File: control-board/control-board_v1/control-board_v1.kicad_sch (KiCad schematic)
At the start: 57 parts, among them J1 Barrel_Jack, J2 Header-M_2x6, J3 Header-M_2x6, J4 Header-M_2x6, J5 Header-M_2x6, J6 Header_1x8, J7 Header_1x8, J8 Header_1x10, J9 Header_1x8, Q1 PMOS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

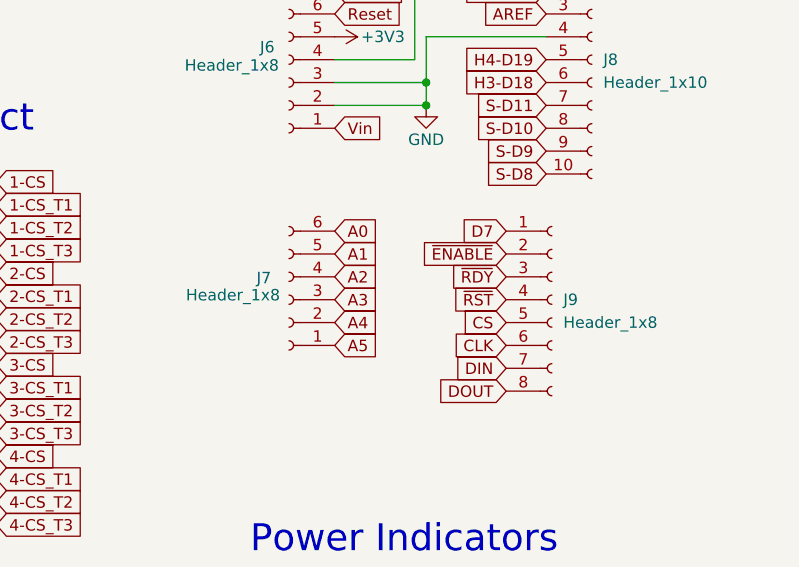
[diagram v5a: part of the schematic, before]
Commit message: pulldown resistor
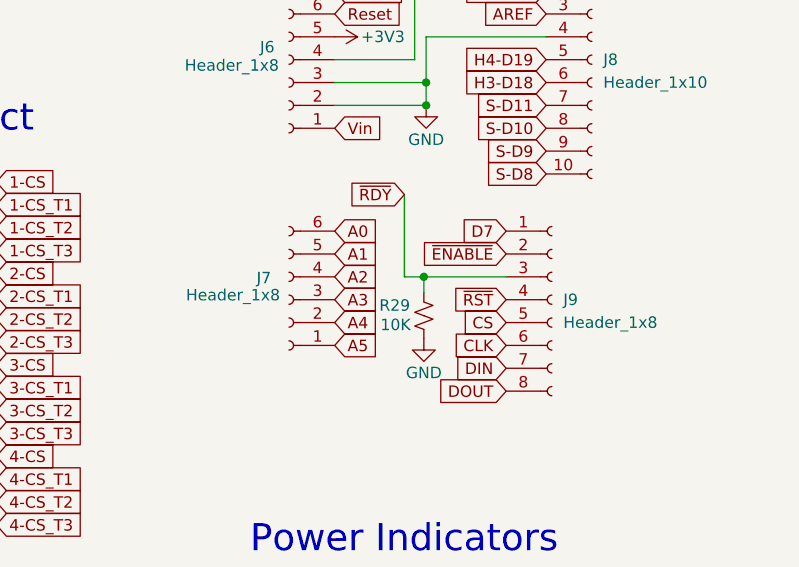
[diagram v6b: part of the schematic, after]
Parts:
- added R29: 10K, Resistor_SMD:R_0805_2012Metric, symbol Device:R_Small_US
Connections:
- net GND: now also R29.2
- net ~{RDY}: now also R29.1
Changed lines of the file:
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@@
   (junction (at 252.349 82.169) (diameter 0) (color 0 0 0 0)
   )
+  (junction (at 252.095 101.219) (diameter 0) (color 0 0 0 0)
+  )
   (junction (at 187.452 91.948) (diameter 0) (color 0 0 0 0)
   )
   (no_connect (at 100.457 118.491))
+  (wire (pts (xy 249.936 101.219) (xy 252.095 101.219))
+    (stroke (width 0) (type default))
+  )
   (wire (pts (xy 179.197 91.948) (xy 178.435 91.948))
     (stroke (width 0) (type default))
@@
     (stroke (width 0) (type default))
   )
+  (wire (pts (xy 252.095 101.219) (xy 261.239 101.219))
+    (stroke (width 0) (type default))
+  )
   (wire (pts (xy 185.928 127.508) (xy 187.452 127.508))
     (stroke (width 0) (type default))
@@
     (stroke (width 0) (type default))
   )
+  (wire (pts (xy 252.095 102.997) (xy 252.095 101.219))
+    (stroke (width 0) (type default))
+  )
   (wire (pts (xy 252.349 82.169) (xy 252.349 79.629))
     (stroke (width 0) (type default))
@@
     (stroke (width 0) (type default))
   )
+  (wire (pts (xy 249.936 92.075) (xy 249.936 101.219))
+    (stroke (width 0) (type default))
+  )
   (wire (pts (xy 266.827 31.369) (xy 270.002 31.369))
     (stroke (width 0) (type default))
@@
     )
   )
-  (global_label "~{RDY}" (shape input) (at 261.239 101.219 180) (fields_autoplaced)
+  (global_label "~{RDY}" (shape input) (at 249.936 92.075 180) (fields_autoplaced)
     (effects (font (size 1.27 1.27)) (justify right))
-    (property "Intersheetrefs" "${INTERSHEET_REFS}" (at 254.6252 101.219 0)
+    (property "Intersheetrefs" "${INTERSHEET_REFS}" (at 243.3222 92.075 0)
       (effects (font (size 1.27 1.27)) (justify right) hide)
     )
@@
     )
   )
+  (symbol (lib_id "power:GND") (at 252.095 108.077 0) (unit 1)
+    (in_bom yes) (on_board yes) (dnp no)
+    (property "Reference" "#PWR046" (at 252.095 114.427 0)
+      (effects (font (size 1.27 1.27)) hide)
+    )
+    (property "Value" "GND" (at 252.095 111.887 0)
+      (effects (font (size 1.27 1.27)))
+    )
+    (property "Footprint" "" (at 252.095 108.077 0)
+      (effects (font (size 1.27 1.27)) hide)
+    )
+    (property "Datasheet" "" (at 252.095 108.077 0)
+      (effects (font (size 1.27 1.27)) hide)
+    )
+    (pin "1")
+    (instances
+      (project "control-board_v1"
+        (path "/5ea0e920-d127-456d-9ad4-df9bbc649b9b"
+          (reference "#PWR046") (unit 1)
+        )
+      )
+      (project "arduino_uno"
+        (path "/b1128066-0aeb-425d-915d-968e839977c3"
+          (reference "#PWR046") (unit 1)
+        )
+      )
+    )
+  )
   (symbol (lib_id "Connector:Conn_01x08_Socket") (at 237.109 77.089 180) (unit 1)
     (in_bom yes) (on_board yes) (dnp no)
@@
         )
       )
+    )
+  )
+  (symbol (lib_id "Device:R_Small_US") (at 252.095 105.537 0) (unit 1)
+    (in_bom yes) (on_board yes) (dnp no)
+    (property "Reference" "R29" (at 247.142 104.394 0)
+      (effects (font (size 1.27 1.27)) (justify left))
+    )
+    (property "Value" "10K" (at 247.269 106.553 0)
+      (effects (font (size 1.27 1.27)) (justify left))
+    )
+    (property "Footprint" "Resistor_SMD:R_0805_2012Metric" (at 252.095 105.537 0)
+      (effects (font (size 1.27 1.27)) hide)
+    )
+    (property "Datasheet" "~" (at 252.095 105.537 0)
+      (effects (font (size 1.27 1.27)) hide)
+    )
+    (pin "1")
+    (pin "2")
+    (instances
+      (project "control-board_v1"
+        (path "/5ea0e920-d127-456d-9ad4-df9bbc649b9b"
+          (reference "R29") (unit 1)
+        )
+      )

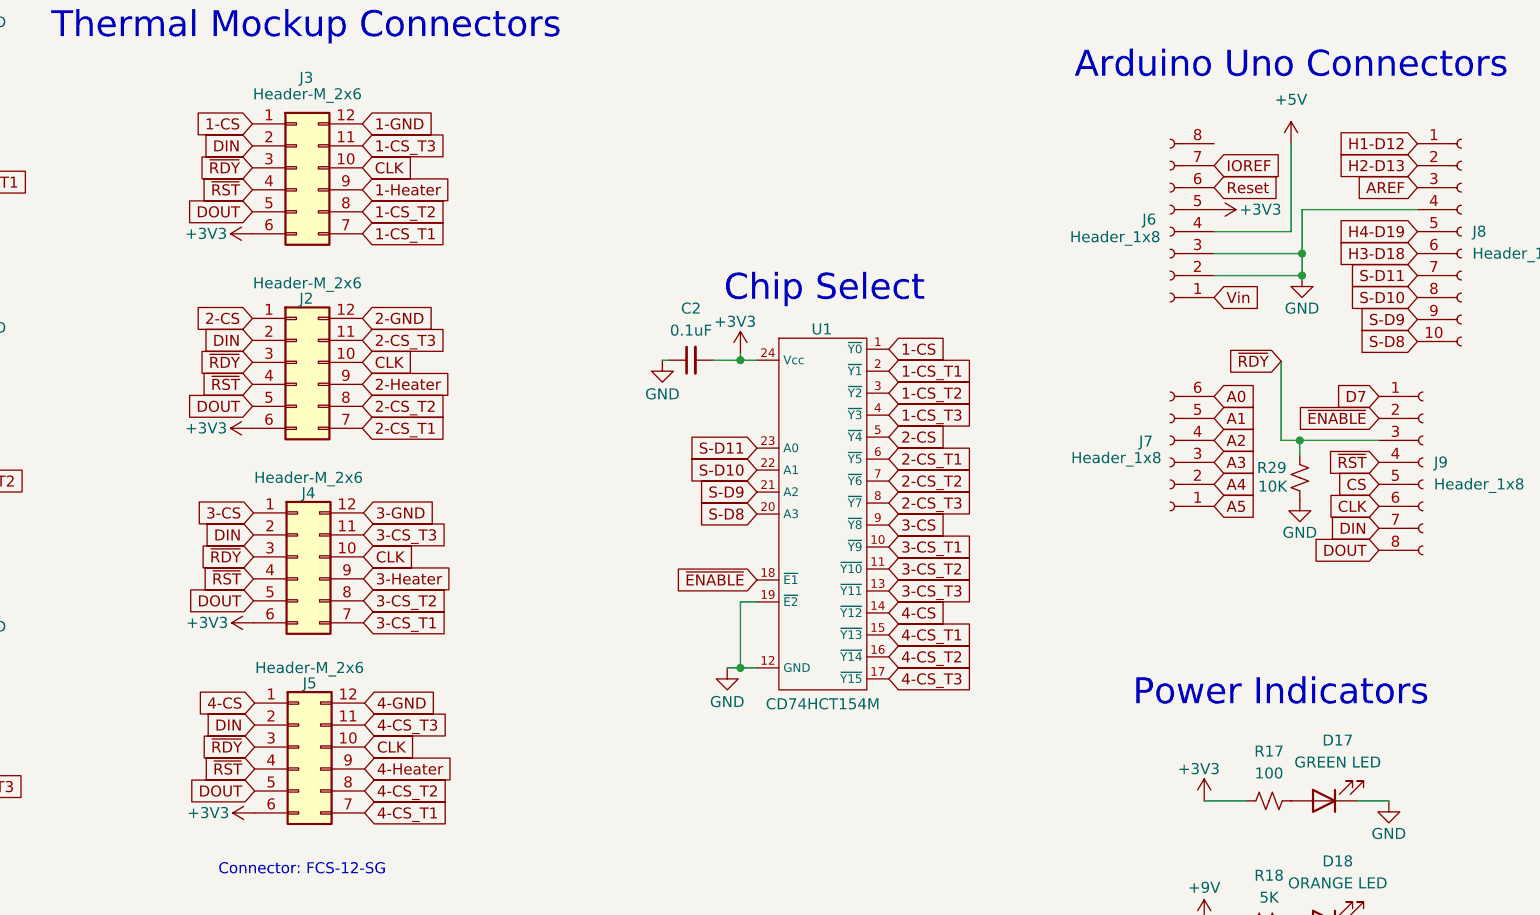
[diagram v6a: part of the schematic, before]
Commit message: fixed RDYB logic in pcb
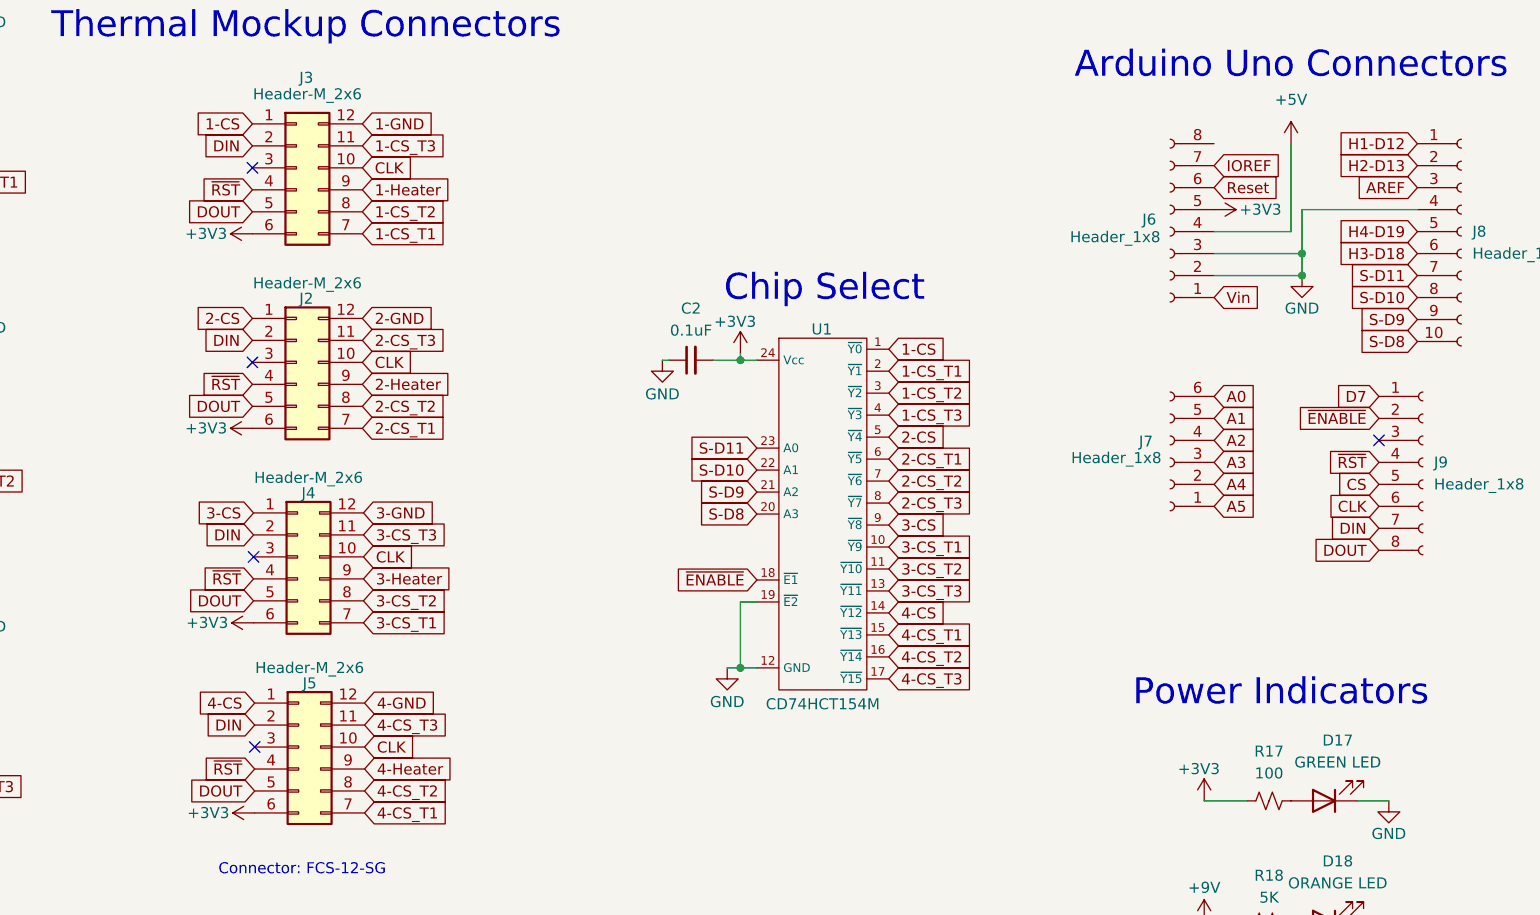
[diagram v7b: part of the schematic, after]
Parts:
- removed R29: 10K, Resistor_SMD:R_0805_2012Metric, symbol Device:R_Small_US
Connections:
- removed net ~{RDY}: J2.3 (Pin_3), J3.3 (Pin_3), J4.3 (Pin_3), J5.3 (Pin_3), J9.3 (Pin_3)
- no-connect marks 1 -> 6
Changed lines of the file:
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@@
   (junction (at 252.349 82.169) (diameter 0) (color 0 0 0 0)
   )
-  (junction (at 252.095 101.219) (diameter 0) (color 0 0 0 0)
-  )
   (junction (at 187.452 91.948) (diameter 0) (color 0 0 0 0)
   )
   (no_connect (at 100.457 118.491))
-  (wire (pts (xy 249.936 101.219) (xy 252.095 101.219))
-    (stroke (width 0) (type default))
-  )
+  (no_connect (at 131.064 69.723))
+  (no_connect (at 131.191 114.681))
+  (no_connect (at 131.318 136.652))
+  (no_connect (at 261.239 101.219))
+  (no_connect (at 131.064 92.202))
   (wire (pts (xy 179.197 91.948) (xy 178.435 91.948))
     (stroke (width 0) (type default))
@@
     (stroke (width 0) (type default))
   )
-  (wire (pts (xy 252.095 101.219) (xy 261.239 101.219))
-    (stroke (width 0) (type default))
-  )
   (wire (pts (xy 185.928 127.508) (xy 187.452 127.508))
     (stroke (width 0) (type default))
@@
     (stroke (width 0) (type default))
   )
-  (wire (pts (xy 252.095 102.997) (xy 252.095 101.219))
-    (stroke (width 0) (type default))
-  )
   (wire (pts (xy 252.349 82.169) (xy 252.349 79.629))
     (stroke (width 0) (type default))
@@
     (stroke (width 0) (type default))
   )
-  (wire (pts (xy 249.936 92.075) (xy 249.936 101.219))
-    (stroke (width 0) (type default))
-  )
   (wire (pts (xy 266.827 31.369) (xy 270.002 31.369))
     (stroke (width 0) (type default))
@@
     )
   )
-  (global_label "~{RDY}" (shape input) (at 131.064 69.723 180) (fields_autoplaced)
-    (effects (font (size 1.27 1.27)) (justify right))
-    (property "Intersheetrefs" "${INTERSHEET_REFS}" (at 124.4502 69.723 0)
-      (effects (font (size 1.27 1.27)) (justify right) hide)
-    )
-  )
   (global_label "S-D10" (shape input) (at 265.684 84.709 180) (fields_autoplaced)
     (effects (font (size 1.27 1.27)) (justify right))
@@
     )
   )
-  (global_label "~{RDY}" (shape input) (at 131.318 136.652 180) (fields_autoplaced)
-    (effects (font (size 1.27 1.27)) (justify right))
-    (property "Intersheetrefs" "${INTERSHEET_REFS}" (at 124.7042 136.652 0)
-      (effects (font (size 1.27 1.27)) (justify right) hide)
-    )
-  )
   (global_label "2-CS" (shape input) (at 204.597 100.838 0) (fields_autoplaced)
     (effects (font (size 1.27 1.27)) (justify left))
@@
     )
   )
-  (global_label "~{RDY}" (shape input) (at 131.064 92.202 180) (fields_autoplaced)
-    (effects (font (size 1.27 1.27)) (justify right))
-    (property "Intersheetrefs" "${INTERSHEET_REFS}" (at 124.4502 92.202 0)
-      (effects (font (size 1.27 1.27)) (justify right) hide)
-    )
-  )
   (global_label "DOUT" (shape input) (at 131.064 97.282 180) (fields_autoplaced)
     (effects (font (size 1.27 1.27)) (justify right))
@@
     )
   )
-  (global_label "~{RDY}" (shape input) (at 131.191 114.681 180) (fields_autoplaced)
-    (effects (font (size 1.27 1.27)) (justify right))
-    (property "Intersheetrefs" "${INTERSHEET_REFS}" (at 124.5772 114.681 0)
-      (effects (font (size 1.27 1.27)) (justify right) hide)
-    )
-  )
   (global_label "3-Heater" (shape input) (at 143.891 117.221 0) (fields_autoplaced)
     (effects (font (size 1.27 1.27)) (justify left))
@@
     )
   )
-  (global_label "~{RDY}" (shape input) (at 249.936 92.075 180) (fields_autoplaced)
-    (effects (font (size 1.27 1.27)) (justify right))
-    (property "Intersheetrefs" "${INTERSHEET_REFS}" (at 243.3222 92.075 0)
-      (effects (font (size 1.27 1.27)) (justify right) hide)
-    )
-  )
   (symbol (lib_id "power:+5V") (at 87.376 136.144 0) (unit 1)
     (in_bom yes) (on_board yes) (dnp no) (fields_autoplaced)
@@
     )
   )
-  (symbol (lib_id "power:GND") (at 252.095 108.077 0) (unit 1)
-    (in_bom yes) (on_board yes) (dnp no)
-    (property "Reference" "#PWR046" (at 252.095 114.427 0)
-      (effects (font (size 1.27 1.27)) hide)
-    )
-    (property "Value" "GND" (at 252.095 111.887 0)
-      (effects (font (size 1.27 1.27)))
-    )
-    (property "Footprint" "" (at 252.095 108.077 0)
-      (effects (font (size 1.27 1.27)) hide)
-    )
-    (property "Datasheet" "" (at 252.095 108.077 0)
-      (effects (font (size 1.27 1.27)) hide)
-    )
-    (pin "1")
-    (instances
-      (project "control-board_v1"
-        (path "/5ea0e920-d127-456d-9ad4-df9bbc649b9b"
-          (reference "#PWR046") (unit 1)
-        )
-      )
-      (project "arduino_uno"
-        (path "/b1128066-0aeb-425d-915d-968e839977c3"
-          (reference "#PWR046") (unit 1)
-        )
-      )
-    )
-  )
   (symbol (lib_id "Connector:Conn_01x08_Socket") (at 237.109 77.089 180) (unit 1)
     (in_bom yes) (on_board yes) (dnp no)
@@
         )
       )
-    )
-  )
-  (symbol (lib_id "Device:R_Small_US") (at 252.095 105.537 0) (unit 1)
-    (in_bom yes) (on_board yes) (dnp no)
-    (property "Reference" "R29" (at 247.142 104.394 0)
-      (effects (font (size 1.27 1.27)) (justify left))
-    )
-    (property "Value" "10K" (at 247.269 106.553 0)
-      (effects (font (size 1.27 1.27)) (justify left))
-    )
-    (property "Footprint" "Resistor_SMD:R_0805_2012Metric" (at 252.095 105.537 0)
-      (effects (font (size 1.27 1.27)) hide)
-    )
-    (property "Datasheet" "~" (at 252.095 105.537 0)
-      (effects (font (size 1.27 1.27)) hide)
-    )
-    (pin "1")
-    (pin "2")
-    (instances
-      (project "control-board_v1"
-        (path "/5ea0e920-d127-456d-9ad4-df9bbc649b9b"
-          (reference "R29") (unit 1)
-        )
-      )

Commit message: additional notes
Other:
- added sheet Test-v1 (Test-v1.kicad_sch)
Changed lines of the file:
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@@
+    )
+  )
+  (sheet (at 56.134 169.037) (size 34.925 23.495) (fields_autoplaced)
+    (stroke (width 0.1524) (type solid))
+    (fill (color 0 0 0 0.0000))
+    (property "Sheetname" "Test-v1" (at 56.134 168.3254 0)
+      (effects (font (size 1.27 1.27)) (justify left bottom))
+    )
+    (property "Sheetfile" "Test-v1.kicad_sch" (at 56.134 193.1166 0)
+      (effects (font (size 1.27 1.27)) (justify left top))
+    )
+    (instances
+      (project "control-board_v1"
+        (path "/5ea0e920-d127-456d-9ad4-df9bbc649b9b" (page "3"))
+      )
     )
   )
